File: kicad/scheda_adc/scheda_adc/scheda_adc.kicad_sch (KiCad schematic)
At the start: 7 parts

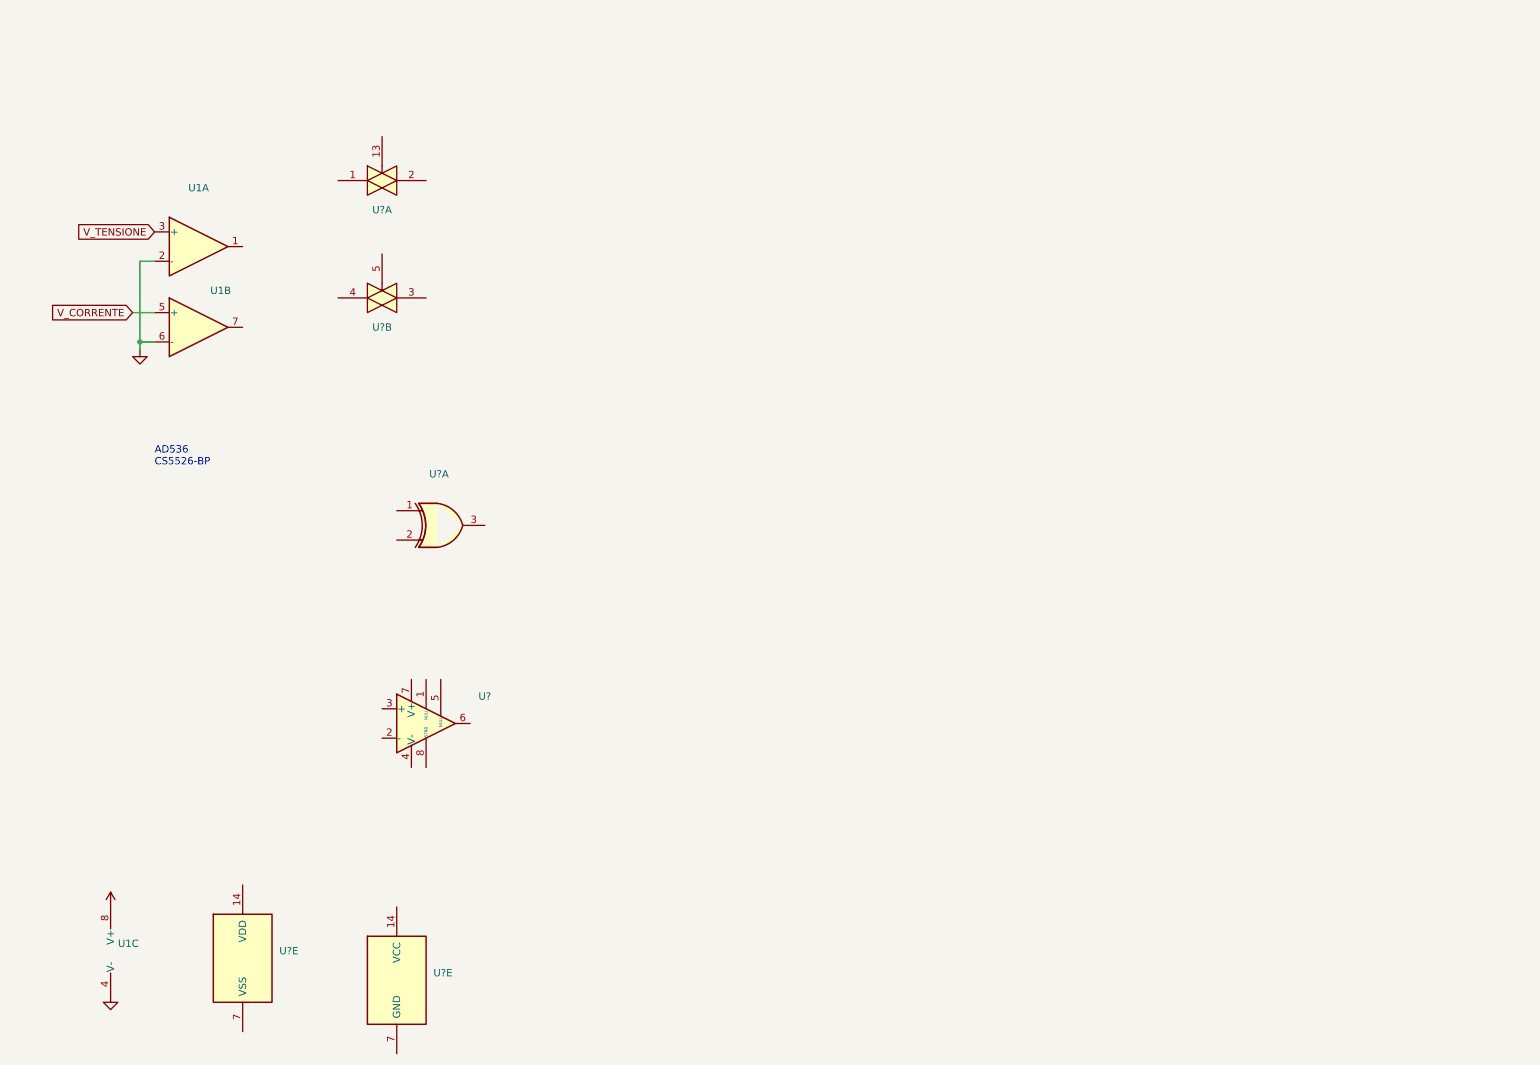
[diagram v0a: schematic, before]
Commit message: schema elettrico misura fase
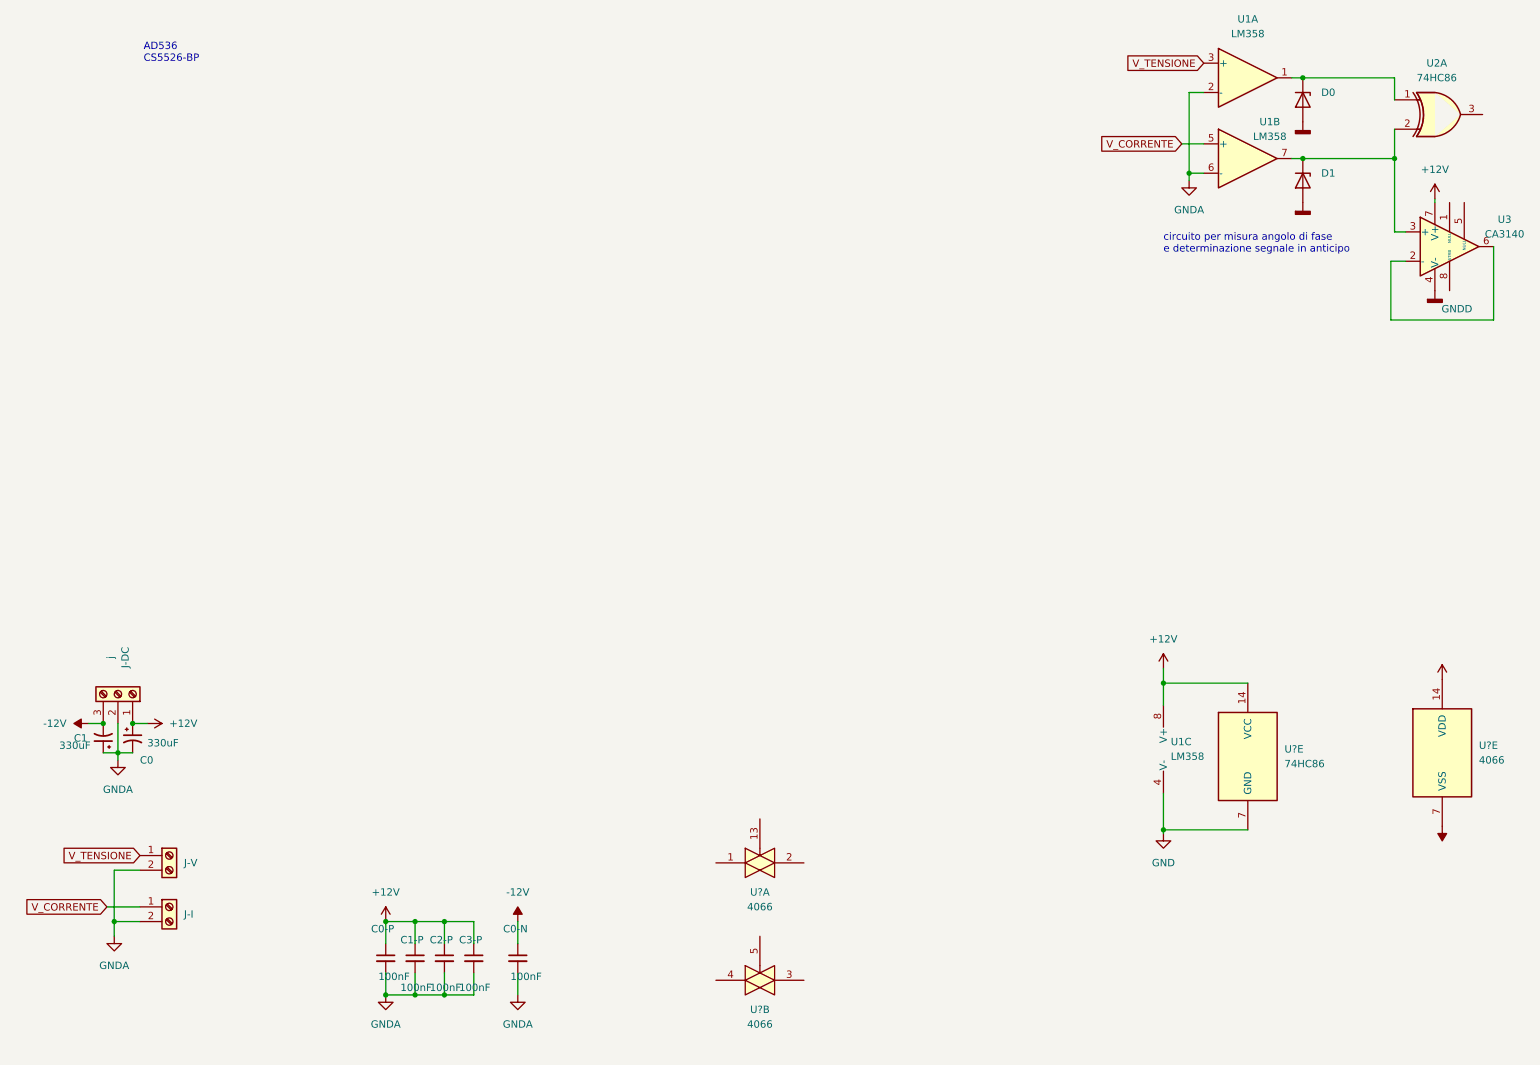
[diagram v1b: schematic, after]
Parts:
- added C0, C1: 330uF, Capacitor_THT:CP_Radial_D10.0mm_P5.00mm, symbol Device:C_Polarized_Small_US
- added C0-N, C0-P, C1-P, C2-P, C3-P: 100nF, Capacitor_THT:C_Disc_D3.0mm_W2.0mm_P2.50mm, symbol Device:C_Small
- added D0, D1: (no value), symbol Device:D_Zener
- added J-DC: j, TerminalBlock_Phoenix:TerminalBlock_Phoenix_MKDS-1,5-3-5.08_1x03_P5.08mm_Horizontal, symbol Connector:Screw_Terminal_01x03
- added J-I, J-V: (no value), symbol Connector:Screw_Terminal_01x02
- U1: value (none) -> LM358
- U2: renamed from U?; value (none) -> 74HC86
- U3: renamed from U?; value (none) -> CA3140
- U? (x3): value (none) -> 4066
- U?: value (none) -> 74HC86
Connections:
- net +12V: now also U3.7 (V+), U?.14 (VCC), U?.14 (VDD), C0-P.1, C0.1, C1-P.1, C2-P.1, C3-P.1, J-DC.1 (Pin_1)
- net GND: now also U?.7 (GND); no longer U1.2 (-), U1.6 (-)
- net V_CORRENTE: now also J-I.1 (Pin_1)
- net V_TENSIONE: now also J-V.1 (Pin_1)
- net at U1.1: now also U2.1, D0.1 (K)
- net at U1.7: now also U2.2, U3.3 (+), D1.1 (K)
- net -12V: now reaches U?.7 (VSS)
- net -12V: now also C0-N.1, C1.2, J-DC.3 (Pin_3)
- net at U3.2 (-): now also U3.6
- net GNDD: now reaches U3.4 (V-)
- net GNDD: now also D0.2 (A), D1.2 (A)
- new net GNDA: C0-N.2, C0-P.2, C0.2, C1-P.2, C1.1, C2-P.2, C3-P.2, J-DC.2 (Pin_2), J-I.2 (Pin_2), J-V.2 (Pin_2), U1.2 (-), U1.6 (-)
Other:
- note added: "circuito per misura angolo di fase e determinazione segnale in anticipo"
- moved on the sheet: U1A, U1B, U1C, U2A, U3, U?A, U?B, U?E

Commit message: continuazione documentazione corrente (todo 3d)
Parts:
- removed C0-N, C0-P, C1-P, C2-P, C3-P: 100nF, Capacitor_THT:C_Disc_D3.0mm_W2.0mm_P2.50mm, symbol Device:C_Small
- removed U2, U?: 74HC86, symbol 74xx:74HC86
- added C0-N1, C0-P1, C1-N1, C1-P1, C2-P1, C3-N1, C3-P1, C4-P1: 100nF, Capacitor_THT:C_Disc_D3.0mm_W2.0mm_P2.50mm, symbol Device:C_Small
- added C2: (no value), symbol Device:C_Polarized_Small
- added C3: 330nF, Capacitor_THT:C_Disc_D3.0mm_W2.0mm_P2.50mm, symbol Device:C
- added C4: 100nF, Capacitor_THT:C_Disc_D3.0mm_W2.0mm_P2.50mm, symbol Device:C
- added C5: 47uF, Capacitor_THT:CP_Radial_D4.0mm_P1.50mm, symbol Device:C_Polarized_Small_US
- added D2: (no value), symbol Diode:1N4007
- added D3: 1N4007, Diode_THT:D_DO-41_SOD81_P10.16mm_Horizontal, symbol Diode:1N4007
- added D4, D5: 1N4001, Diode_THT:D_DO-41_SOD81_P10.16mm_Horizontal, symbol Diode:1N4001
- added J1: (no value), symbol Connector:Conn_01x07_Male
- added R0, R1, R2, R3: (no value), symbol Device:R
- added U2: (no value), symbol 4xxx:4070
- added unit 3 of U3
- added U4: (no value), symbol simboli_tesina:AD536A
- added U5: (no value), Package_TO_SOT_THT:TO-220-3_Vertical, symbol Regulator_Linear:L7808
- U1: value LM358 -> (none)
- U3: renamed from U?; value 4066 -> (none)
- U6: renamed from U3; value CA3140 -> (none)
- renumbered J-DC to J-DC1, J-I to J-I1, J-V to J-V1
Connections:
- net GND is gone; now on net -12V: U1.4 (V-)
- net GNDD is gone; now on net GNDA: D0.2 (A), D1.2 (A), U6.4 (V-)
- net +12V: now also C0-P1.1, C1-P1.1, C2-P1.1, C2.1, C3-P1.1, C3.1, C4-P1.1, D4.1 (K), U2.14 (VDD), U4.14 (Vs+), U5.1 (IN)
- net -12V: now also C0-N1.1, C1-N1.1, C3-N1.1, U4.3 (Vs-)
- net GNDA: now also C0-N1.2, C0-P1.2, C1-N1.2, C1-P1.2, C2-P1.2, C3-N1.2, C3-P1.2, C3.2, C4-P1.2, C4.2, C5.2, D2.2 (A), D3.2 (A), D5.2 (A), J1.2 (Pin_2), R3.2, U2.7 (VSS), U4.10 (COM), U4.9 (Rl), U5.2 (GND)
- net V_CORRENTE: now also U1.3 (+), U3.4; no longer U1.5 (+)
- net V_TENSIONE: now also U1.5 (+), U3.1; no longer U1.3 (+)
- net EN_V: now reaches U3.13
- net EN_V: now also J1.5 (Pin_5)
- net at U3.2: now also U3.3, U3.9, U4.1 (Vin)
- net at U1.1: now also D2.1 (K), U2.1; no longer D0.1 (K)
- net at U1.7, U6.3 (+): now also D3.1 (K), U2.2; no longer D1.1 (K)
- net EN_I: now reaches U3.5
- net EN_I: now also J1.4 (Pin_4)
- net at U6.2 (-), U6.6: now also R1.1
- new net: R0.1, U2.3
- new net: R2.1, U4.6 (Vout)
- new net: C2.2, U4.4 (Cav)
- new net: U4.7 (Buf_in), U4.8 (Iout)
- new net +5V: C4.1, C5.1, D4.2 (A), D5.1 (K), J1.1 (Pin_1), U5.3 (OUT)
- new net ADC_IN: J1.3 (Pin_3), R2.2, R3.1
- new net EN_P: J1.6 (Pin_6), U3.6
- new net FREQUENCY: D1.1 (K), J1.7 (Pin_7), R1.2
- new net PHASE: D0.1 (K), R0.2, U3.8
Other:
- note added: "circuito per misura angolo di fase e frequenza"
- note removed: "circuito per misura angolo di fase e determinazione segnale in anticipo"
- moved on the sheet: D0, D1, U1A, U1B, U3A, U3B, U3E, U6
